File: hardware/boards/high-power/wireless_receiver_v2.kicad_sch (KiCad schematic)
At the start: 31 parts, among them Q3 SSM3J35AMFV,L3F, Q4 2N7002, Q5 2N7002, U2 BQ51013B

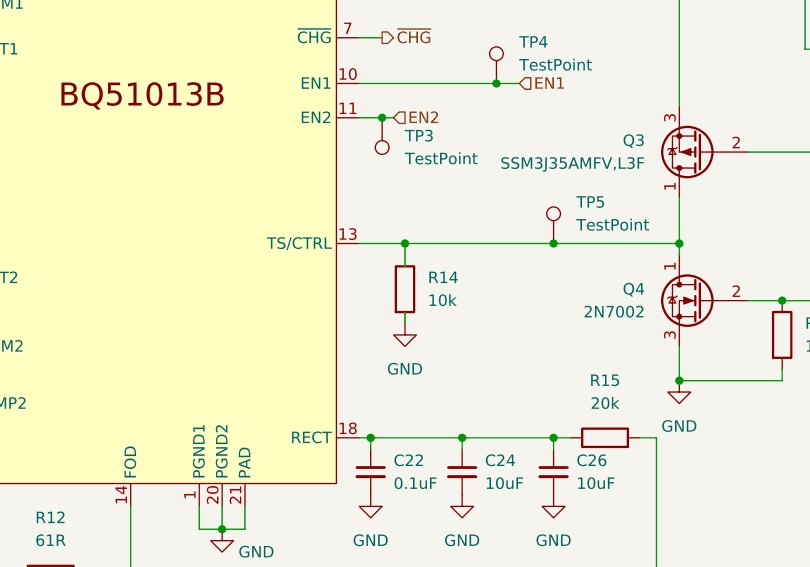
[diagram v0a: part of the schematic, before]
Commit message: Add footprints and models for LP board
Also completed rough layout for LP board to estimate board space usage.
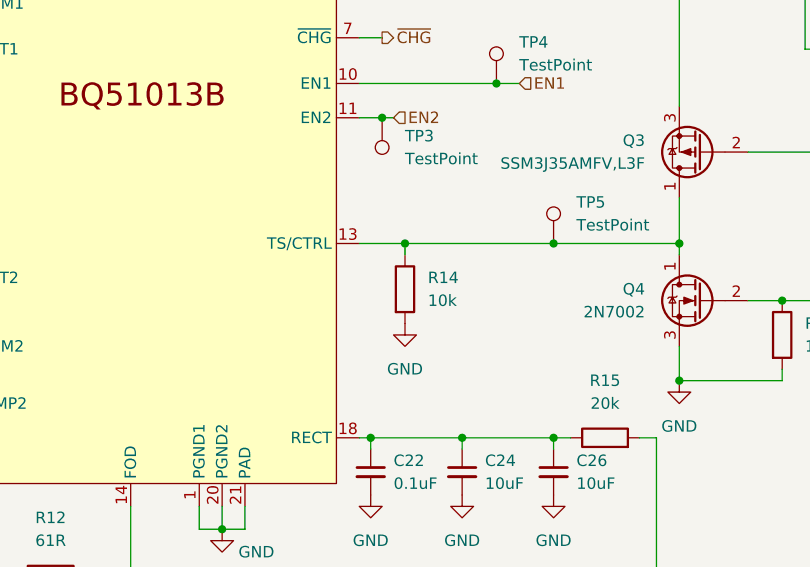
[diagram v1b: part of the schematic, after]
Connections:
- net at Q3.1 (D), Q4.1 (D), TP5.1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: now also R14.1

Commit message: Add initial changes after schematic review
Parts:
- added R305, R309, R310: 10k, symbol Device:R
- C307: renamed from C17; value 22nF -> 47nF
- C310: renamed from C20; value 22nF -> 47nF
- R301: renamed from R12; value 61R -> 66R
- renumbered C11 to C301, C12 to C302, C13 to C303, C14 to C304, C15 to C305, C16 to C306, C18 to C308, C19 to C309, C21 to C311, C22 to C312, C23 to C313, C24 to C314, C25 to C315, C26 to C316, L1 to L301, Q3 to Q301, Q4 to Q302, Q5 to Q303, R13 to R302, R14 to R303, R15 to R304, R16 to R306, R17 to R307, R18 to R308, TP3 to TP301, TP4 to TP302, TP5 to TP303, U2 to U301
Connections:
- net EN1: now also R309.2
- net EN2: now also R310.2
- net ~{CHG}: now also R305.2
- new net +3.3V: R305.1, R309.1, R310.1
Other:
- moved on the sheet: C313, C315, R307, TP301, TP302
